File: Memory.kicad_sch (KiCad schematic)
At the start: 16 parts, among them IC1 NAND_MT29F1G08ABAEAWP-IT_E_TR

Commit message: Update
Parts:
- removed C18, C20: 2u2, Capacitor_SMD:C_0603_1608Metric, symbol Device:C
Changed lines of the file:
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@@
 	)
 	(junction
-		(at 146.05 77.47)
-		(diameter 0)
-		(color 0 0 0 0)
-	)
-	(junction
 		(at 281.94 74.93)
 		(diameter 0)
@@
 	)
 	(junction
-		(at 146.05 90.17)
-		(diameter 0)
-		(color 0 0 0 0)
-	)
-	(junction
 		(at 273.05 74.93)
 		(diameter 0)
@@
 	)
 	(junction
-		(at 154.94 90.17)
-		(diameter 0)
-		(color 0 0 0 0)
-	)
-	(junction
 		(at 128.27 77.47)
 		(diameter 0)
@@
 	)
 	(junction
-		(at 154.94 77.47)
-		(diameter 0)
-		(color 0 0 0 0)
-	)
-	(junction
 		(at 185.42 127)
 		(diameter 0)
@@
 	(wire
 		(pts
-			(xy 154.94 77.47) (xy 154.94 80.01)
-		)
-		(stroke
-			(width 0)
-			(type default)
-		)
-	)
-	(wire
-		(pts
 			(xy 185.42 172.72) (xy 185.42 177.8)
 		)
@@
 	(wire
 		(pts
-			(xy 154.94 77.47) (xy 146.05 77.47)
-		)
-		(stroke
-			(width 0)
-			(type default)
-		)
-	)
-	(wire
-		(pts
 			(xy 142.24 149.86) (xy 163.83 149.86)
 		)
@@
 	(wire
 		(pts
-			(xy 154.94 87.63) (xy 154.94 90.17)
-		)
-		(stroke
-			(width 0)
-			(type default)
-		)
-	)
-	(wire
-		(pts
 			(xy 119.38 87.63) (xy 119.38 90.17)
 		)
@@
 	(wire
 		(pts
-			(xy 163.83 80.01) (xy 163.83 77.47)
-		)
-		(stroke
-			(width 0)
-			(type default)
-		)
-	)
-	(wire
-		(pts
 			(xy 304.8 138.43) (xy 336.55 138.43)
 		)
@@
 	(wire
 		(pts
-			(xy 163.83 77.47) (xy 154.94 77.47)
-		)
-		(stroke
-			(width 0)
-			(type default)
-		)
-	)
-	(wire
-		(pts
 			(xy 74.93 111.76) (xy 74.93 106.68)
 		)
@@
 	(wire
 		(pts
-			(xy 163.83 90.17) (xy 154.94 90.17)
-		)
-		(stroke
-			(width 0)
-			(type default)
-		)
-	)
-	(wire
-		(pts
 			(xy 142.24 167.64) (xy 163.83 167.64)
 		)
@@
 	(wire
 		(pts
-			(xy 154.94 90.17) (xy 146.05 90.17)
-		)
-		(stroke
-			(width 0)
-			(type default)
-		)
-	)
-	(wire
-		(pts
 			(xy 142.24 165.1) (xy 163.83 165.1)
 		)
@@
 	(wire
 		(pts
-			(xy 163.83 87.63) (xy 163.83 90.17)
-		)
-		(stroke
-			(width 0)
-			(type default)
-		)
-	)
-	(wire
-		(pts
 			(xy 110.49 77.47) (xy 110.49 80.01)
 		)
@@
 	)
 	(symbol
-		(lib_id "Device:C")
-		(at 154.94 83.82 0)
-		(unit 1)
-		(exclude_from_sim no)
-		(in_bom yes)
-		(on_board yes)
-		(dnp no)
-		(property "Reference" "C18"
-			(at 155.956 81.534 0)
-			(effects
-				(font
-					(size 1.27 1.27)
-				)
-				(justify left)
-			)
-		)
-		(property "Value" "2u2"
-			(at 155.702 86.106 0)
-			(effects
-				(font
-					(size 1.27 1.27)
-				)
-				(justify left)
-			)
-		)
-		(property "Footprint" "Capacitor_SMD:C_0603_1608Metric"
-			(at 155.9052 87.63 0)
-			(effects
-				(font
-					(size 1.27 1.27)
-				)
-				(hide yes)
-			)
-		)
-		(property "Datasheet" "~"
-			(at 154.94 83.82 0)
-			(effects
-				(font
-					(size 1.27 1.27)
-				)
-				(hide yes)
-			)
-		)
-		(property "Description" "Unpolarized capacitor"
-			(at 154.94 83.82 0)
-			(effects
-				(font
-					(size 1.27 1.27)
-				)
-				(hide yes)
-			)
-		)
-		(pin "2"
-		)
-		(pin "1"
-		)
-		(instances
-			(project "STM32H7_Board"
-				(path "/9b48e30a-b912-4658-a133-1a15707d5b7d/c1273a5b-dc13-48da-a35d-ed40e44ccc48"
-					(reference "C18")
-					(unit 1)
-				)
-			)
-		)
-	)
-	(symbol
 		(lib_id "power:+3.3V")
 		(at 181.61 91.44 0)
@@
 					(unit 1)
 				)
-			)
-		)
-	)
-	(symbol
-		(lib_id "Device:C")
-		(at 163.83 83.82 0)
-		(unit 1)
-		(exclude_from_sim no)
-		(in_bom yes)
-		(on_board yes)
-		(dnp no)
-		(property "Reference" "C20"
-			(at 164.846 81.534 0)
-			(effects
-				(font
-					(size 1.27 1.27)
-				)
-				(justify left)
-			)
-		)
-		(property "Value" "2u2"
-			(at 164.592 86.106 0)
-			(effects
-				(font
-					(size 1.27 1.27)
-				)
-				(justify left)
-			)
-		)
-		(property "Footprint" "Capacitor_SMD:C_0603_1608Metric"
-			(at 164.7952 87.63 0)
-			(effects
-				(font
-					(size 1.27 1.27)
-				)
-				(hide yes)
-			)
-		)
-		(property "Datasheet" "~"
-			(at 163.83 83.82 0)
-			(effects
-				(font
-					(size 1.27 1.27)
-				)
-				(hide yes)
-			)
-		)
-		(property "Description" "Unpolarized capacitor"
-			(at 163.83 83.82 0)
-			(effects
-				(font
-					(size 1.27 1.27)
-				)
-				(hide yes)
-			)
-		)
-		(pin "2"
-		)
-		(pin "1"
-		)
-		(instances
-			(project "STM32H7_Board"
-				(path "/9b48e30a-b912-4658-a133-1a15707d5b7d/c1273a5b-dc13-48da-a35d-ed40e44ccc48"
-					(reference "C20")
-					(unit 1)
-				)

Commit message: Update
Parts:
- IC1: value NAND_MT29F1G08ABAEAWP-IT_E_TR -> NAND_MT29F2G08ABAGAWP-IT:G
- R13: footprint Resistor_SMD:R_0805_2012Metric_1 -> Resistor_SMD:R_0603_1608Metric
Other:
- note added: "MT29F1G08ABAEAWP-ITX:E TR"
- note removed: "0.1µF (100nF) ceramic capacitor per VCC and VCCQ pin Place 100nF capacitors as close as possible to each power pin to filter high-frequency noise. Bulk Capacitor near one of the VCC pins (Pin 38 or Pin 48)."
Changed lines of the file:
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@@
-		)
-	)
-	(text_box "Note:\nSDRAM\n- CKE Clock Enable (LOW) can be put into a low power state To enter a deep sleep Issue a SELF REFRESH command  while CKE is pulled Low\n\nNAND\n- Use FMC_NCE CE Chip Enable (HIGH) to put into low power mode"
-		(exclude_from_sim no)
-		(at 27.94 224.79 0)
-		(size 45.085 45.72)
-		(stroke
-			(width 0)
-			(type dash)
-		)
-		(fill
-			(type none)
-		)
-		(effects
-			(font
-				(size 1 1)
-			)
-			(justify left top)
 		)
 	)
@@
 		)
 	)
-	(text "0.1µF (100nF) ceramic capacitor per VCC and VCCQ pin\nPlace 100nF capacitors as close as possible to each \npower pin to filter high-frequency noise.\nBulk Capacitor near one of the VCC pins (Pin 38 or Pin 48)."
+	(text "MT29F1G08ABAEAWP-ITX:E TR"
 		(exclude_from_sim no)
-		(at 277.368 93.472 0)
+		(at 291.592 105.156 0)
 		(effects
 			(font
 				(size 1 1)
 			)
-			(justify left)
-		)
-	)
-	(label "VDDQ_4"
-		(at 161.29 119.38 180)
-		(fields_autoplaced yes)
-		(effects
-			(font
-				(size 1.27 1.27)
-			)
-			(justify right bottom)
 		)
 	)
@@
 		)
 	)
-	(label "VSSQ_2"
-		(at 93.98 134.62 0)
-		(fields_autoplaced yes)
-		(effects
-			(font
-				(size 1.27 1.27)
-			)
-			(justify left bottom)
-		)
-	)
 	(label "SDRAM_~{CS}"
 		(at 93.98 152.4 0)
@@
 		)
 	)
-	(label "VDD_3"
-		(at 93.98 172.72 0)
-		(fields_autoplaced yes)
-		(effects
-			(font
-				(size 1.27 1.27)
-			)
-			(justify left bottom)
-		)
-	)
 	(label "SDRAM_BA0"
 		(at 93.98 154.94 0)
@@
 		)
 	)
-	(label "VDDQ_2"
-		(at 93.98 127 0)
-		(fields_autoplaced yes)
-		(effects
-			(font
-				(size 1.27 1.27)
-			)
-			(justify left bottom)
-		)
-	)
-	(label "VSSQ_3"
-		(at 161.29 127 180)
-		(fields_autoplaced yes)
-		(effects
-			(font
-				(size 1.27 1.27)
-			)
-			(justify right bottom)
-		)
-	)
 	(label "NAND_CE#"
 		(at 256.54 135.89 0)
@@
 		)
 	)
-	(label "VSSQ_4"
-		(at 161.29 111.76 180)
-		(fields_autoplaced yes)
-		(effects
-			(font
-				(size 1.27 1.27)
-			)
-			(justify right bottom)
-		)
-	)
-	(label "VDD_2"
-		(at 93.98 139.7 0)
-		(fields_autoplaced yes)
-		(effects
-			(font
-				(size 1.27 1.27)
-			)
-			(justify left bottom)
-		)
-	)
-	(label "VDDQ_1"
-		(at 93.98 111.76 0)
-		(fields_autoplaced yes)
-		(effects
-			(font
-				(size 1.27 1.27)
-			)
-			(justify left bottom)
-		)
-	)
 	(label "NAND_D4"
 		(at 313.69 133.35 0)
@@
 		)
 	)
-	(label "VSSQ_1"
-		(at 93.98 119.38 0)
-		(fields_autoplaced yes)
-		(effects
-			(font
-				(size 1.27 1.27)
-			)
-			(justify left bottom)
-		)
-	)
 	(label "SDRAM_DQMH"
 		(at 161.29 144.78 180)
@@
 		)
 	)
-	(label "VSS_1"
-		(at 161.29 172.72 180)
-		(fields_autoplaced yes)
-		(effects
-			(font
-				(size 1.27 1.27)
-			)
-			(justify right bottom)
-		)
-	)
 	(label "NAND_D6"
 		(at 313.69 128.27 0)
@@
 		)
 	)
-	(label "VDDQ_3"
-		(at 161.29 134.62 180)
-		(fields_autoplaced yes)
-		(effects
-			(font
-				(size 1.27 1.27)
-			)
-			(justify right bottom)
-		)
-	)
 	(label "NAND_RE#"
 		(at 256.54 133.35 0)
@@
 		)
 	)
-	(label "VSS_3"
-		(at 161.29 106.68 180)
-		(fields_autoplaced yes)
-		(effects
-			(font
-				(size 1.27 1.27)
-			)
-			(justify right bottom)
-		)
-	)
 	(label "NAND_D1"
 		(at 313.69 161.29 0)
@@
 		)
 	)
-	(label "VSS_2"
-		(at 161.29 139.7 180)
-		(fields_autoplaced yes)
-		(effects
-			(font
-				(size 1.27 1.27)
-			)
-			(justify right bottom)
-		)
-	)
 	(label "SDRAM_DQ4"
 		(at 161.29 132.08 180)
@@
 	(label "SDRAM_DQ3"
 		(at 93.98 132.08 0)
-		(fields_autoplaced yes)
-		(effects
-			(font
-				(size 1.27 1.27)
-			)
-			(justify left bottom)
-		)
-	)
-	(label "VDD_1"
-		(at 93.98 106.68 0)
 		(fields_autoplaced yes)
 		(effects
@@
 			)
 		)
-		(property "Footprint" "Resistor_SMD:R_0805_2012Metric_1"
+		(property "Footprint" "Resistor_SMD:R_0603_1608Metric"
 			(at 266.192 123.19 90)
 			(effects
@@
 			)
 		)
-		(property "Value" "NAND_MT29F1G08ABAEAWP-IT_E_TR"
+		(property "Value" "NAND_MT29F2G08ABAGAWP-IT:G"
 			(at 289.56 110.49 0)
 			(effects

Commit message: Update
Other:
- company: (none) -> Peter Hancak
- title: (none) -> STM32H7S3 Board
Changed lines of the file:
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@@
 	(generator_version "8.0")
 	(paper "A3")
+	(title_block
+		(title "STM32H7S3 Board")
+		(date "2026-03-17")
+		(rev "B")
+		(company "Peter Hancak")
+	)
 	(junction
 		(at 128.27 90.17)

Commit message: Update
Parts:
- SDRAM1: value SDRAM_IS42S83200J-7TLI -> SDRAM_AS4C32M8SA-7TCN
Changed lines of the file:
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@@
 			)
 		)
-		(property "Value" "SDRAM_IS42S83200J-7TLI"
+		(property "Value" "SDRAM_AS4C32M8SA-7TCN"
 			(at 125.73 101.6 0)
 			(effects

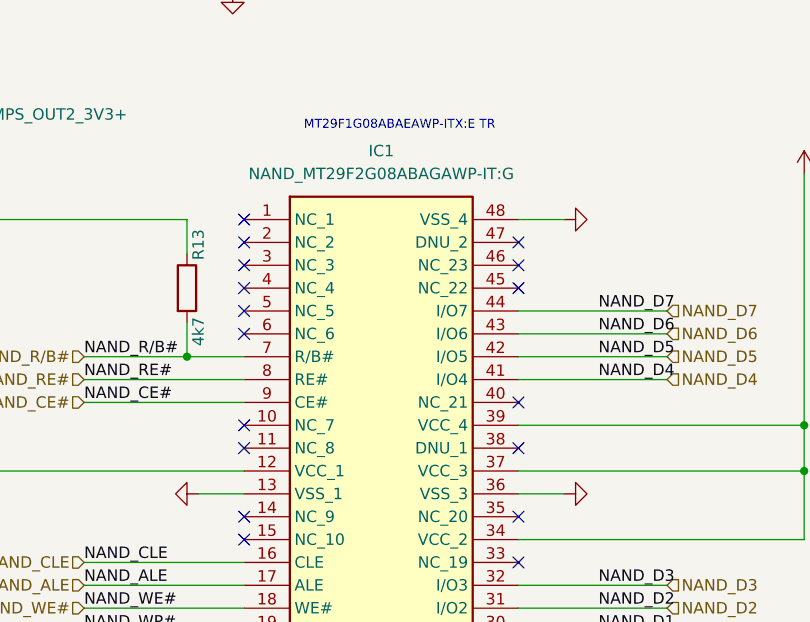
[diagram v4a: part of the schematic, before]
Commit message: NAND Interface
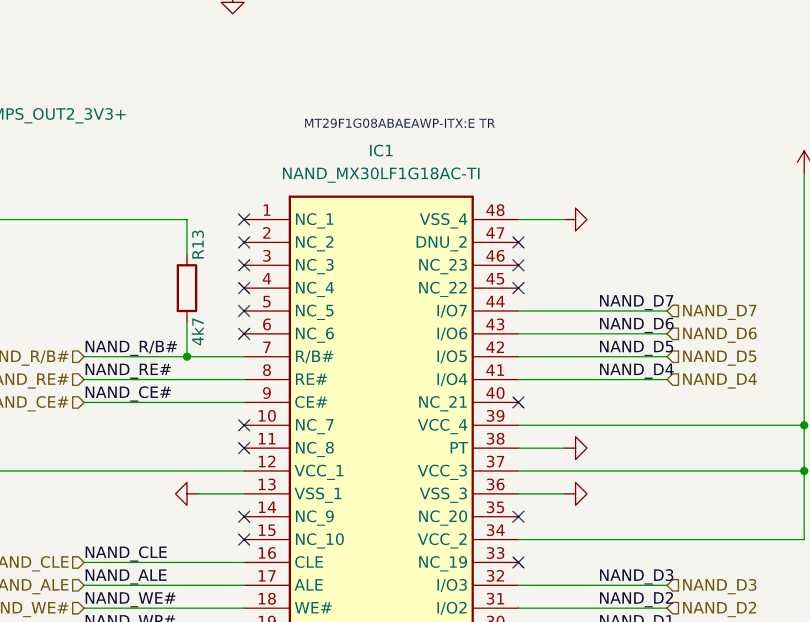
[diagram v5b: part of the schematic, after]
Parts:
- IC1: value NAND_MT29F2G08ABAGAWP-IT:G -> NAND_MX30LF1G18AC-TI
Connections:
- net GND: now also IC1.38 (PT)
- no-connect marks 34 -> 33
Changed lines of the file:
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@@
 	)
 	(no_connect
-		(at 304.8 140.97)
-	)
-	(no_connect
 		(at 304.8 135.89)
 	)
@@
 	(wire
 		(pts
+			(xy 304.8 140.97) (xy 309.88 140.97)
+		)
+		(stroke
+			(width 0)
+			(type default)
+		)
+	)
+	(wire
+		(pts
 			(xy 256.54 156.21) (xy 274.32 156.21)
 		)
@@
 	)
 	(symbol
+		(lib_id "power:GND")
+		(at 309.88 140.97 90)
+		(mirror x)
+		(unit 1)
+		(exclude_from_sim no)
+		(in_bom yes)
+		(on_board yes)
+		(dnp no)
+		(fields_autoplaced yes)
+		(property "Reference" "#PWR056"
+			(at 316.23 140.97 0)
+			(effects
+				(font
+					(size 1.27 1.27)
+				)
+				(hide yes)
+			)
+		)
+		(property "Value" "GND"
+			(at 314.96 140.97 0)
+			(effects
+				(font
+					(size 1.27 1.27)
+				)
+				(hide yes)
+			)
+		)
+		(property "Footprint" ""
+			(at 309.88 140.97 0)
+			(effects
+				(font
+					(size 1.27 1.27)
+				)
+				(hide yes)
+			)
+		)
+		(property "Datasheet" ""
+			(at 309.88 140.97 0)
+			(effects
+				(font
+					(size 1.27 1.27)
+				)
+				(hide yes)
+			)
+		)
+		(property "Description" "Power symbol creates a global label with name \"GND\" , ground"
+			(at 309.88 140.97 0)
+			(effects
+				(font
+					(size 1.27 1.27)
+				)
+				(hide yes)
+			)
+		)
+		(pin "1"
+		)
+		(instances
+			(project "STM32H7_Board"
+				(path "/9b48e30a-b912-4658-a133-1a15707d5b7d/c1273a5b-dc13-48da-a35d-ed40e44ccc48"
+					(reference "#PWR056")
+					(unit 1)
+				)
+			)
+		)
+	)
+	(symbol
 		(lib_id "Device:C")
 		(at 92.71 83.82 0)
@@
 			)
 		)
-		(property "Value" "NAND_MT29F2G08ABAGAWP-IT:G"
+		(property "Value" "NAND_MX30LF1G18AC-TI"
 			(at 289.56 110.49 0)
 			(effects
